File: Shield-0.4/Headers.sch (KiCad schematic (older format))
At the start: 22 parts, among them J1 EXPANSION, J10 E0 COOL, J11 E0 TEMP, J12 E1 H&T, J13 FAN_0, J14 E0 MOT/STOP, J15 E0 MOT/STOP, J18 E3 MOT/STOP, J19 E0 HEAT, J20 E4 MOT/STOP, J21 PWR, J28 Probe, J4 PWR, J5 E2 H&T, J6 SPADE1, J7 SPADE1, J8 E2 MOT/STOP, J9 E1 MOT/STOP, P1 STEP, P2 E0 H&T

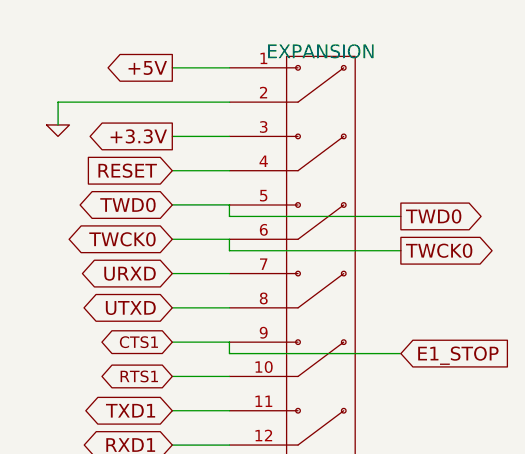
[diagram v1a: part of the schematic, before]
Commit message: Reset pin on the expansion header changed to V_IN now we have a reset pin on the board.  There was no V_IN on that header before, and it would be useful.
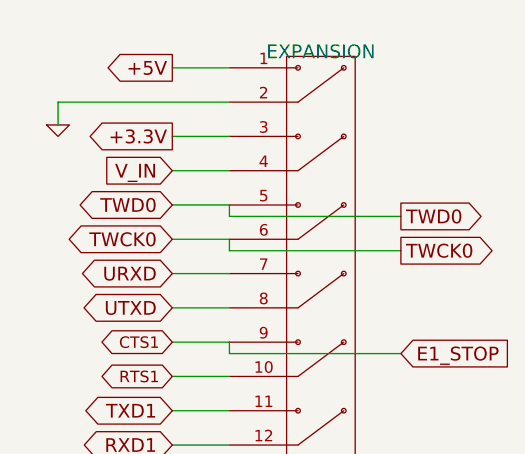
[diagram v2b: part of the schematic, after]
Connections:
- net RESET is gone; now on net V_IN: J1.4
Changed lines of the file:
@@
 Sheet 3 4
 Title "Duet"
-Date "11 jun 2015"
+Date "9 jul 2015"
 Rev "0.7"
 Comp "Think3DPrint3D, RepRapPro"
@@
 Text GLabel 1600 1750 0    60   BiDi ~ 0
 UTXD
-Text GLabel 1600 1150 0    60   Input ~ 0
-RESET
 $Comp
 L CONN7 J9
@@
 Wire Wire Line
 	1600 9650 1800 9650
+Text GLabel 1600 1150 0    60   Input ~ 0
+V_IN
 $EndSCHEMATC
